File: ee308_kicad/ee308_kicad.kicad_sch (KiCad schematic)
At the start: 0 parts

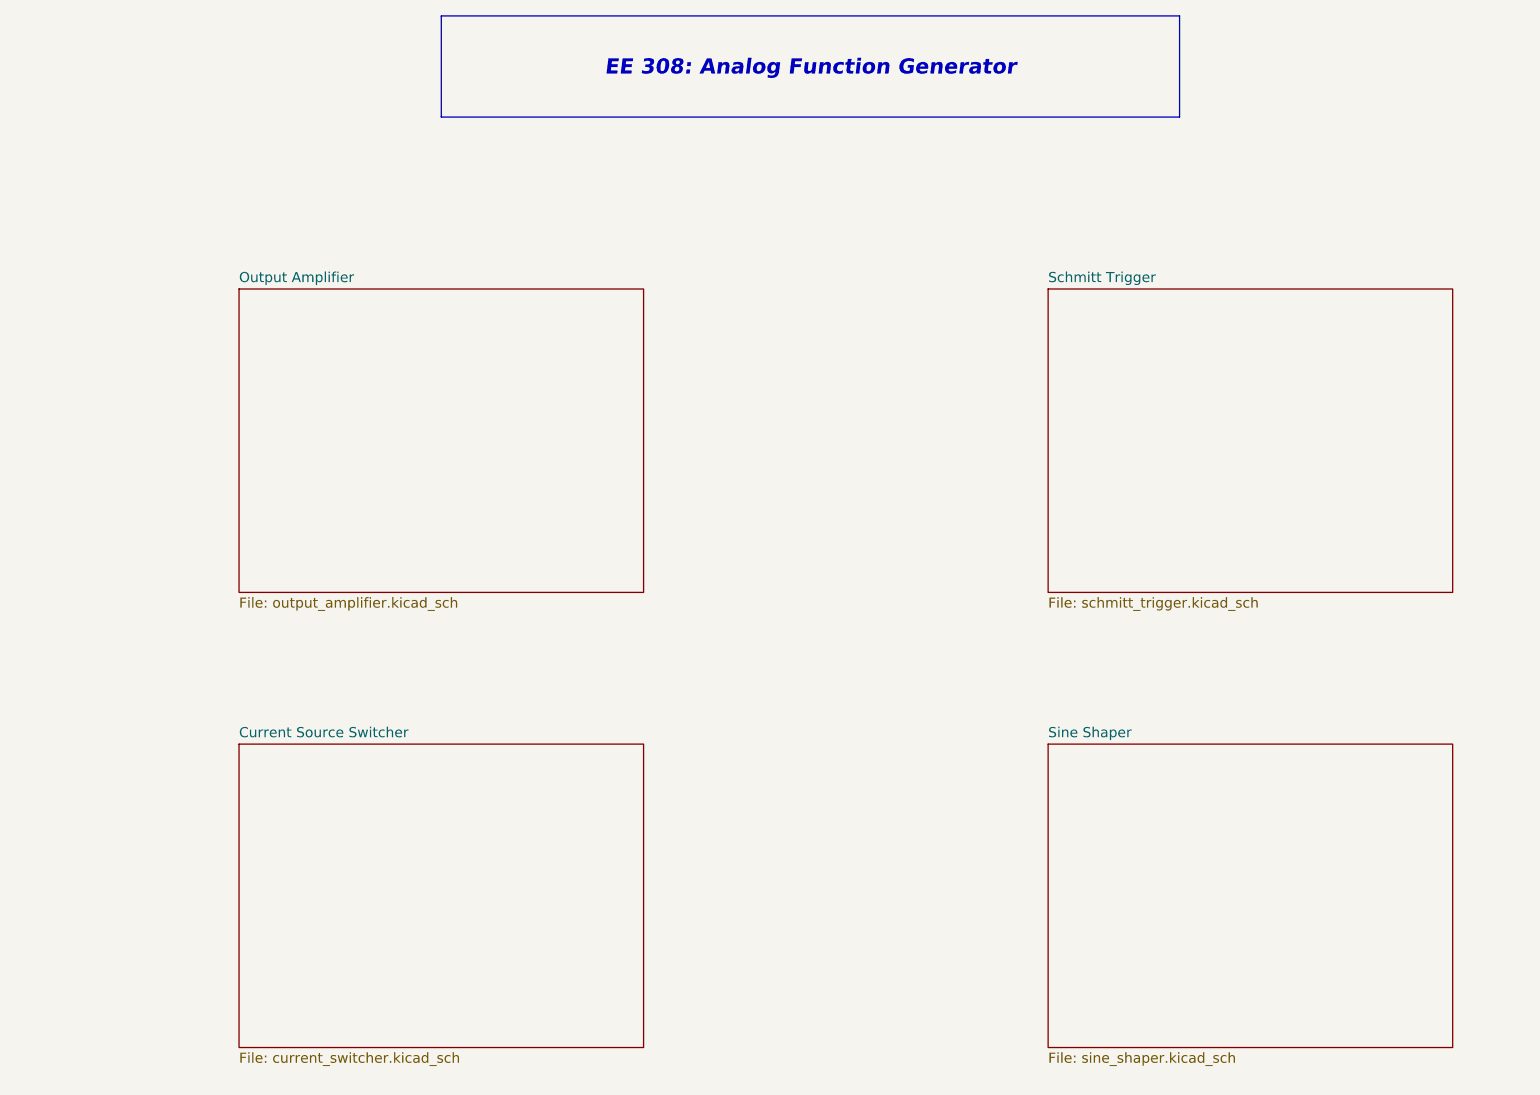
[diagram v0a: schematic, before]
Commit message: Update with current switch/integrator.
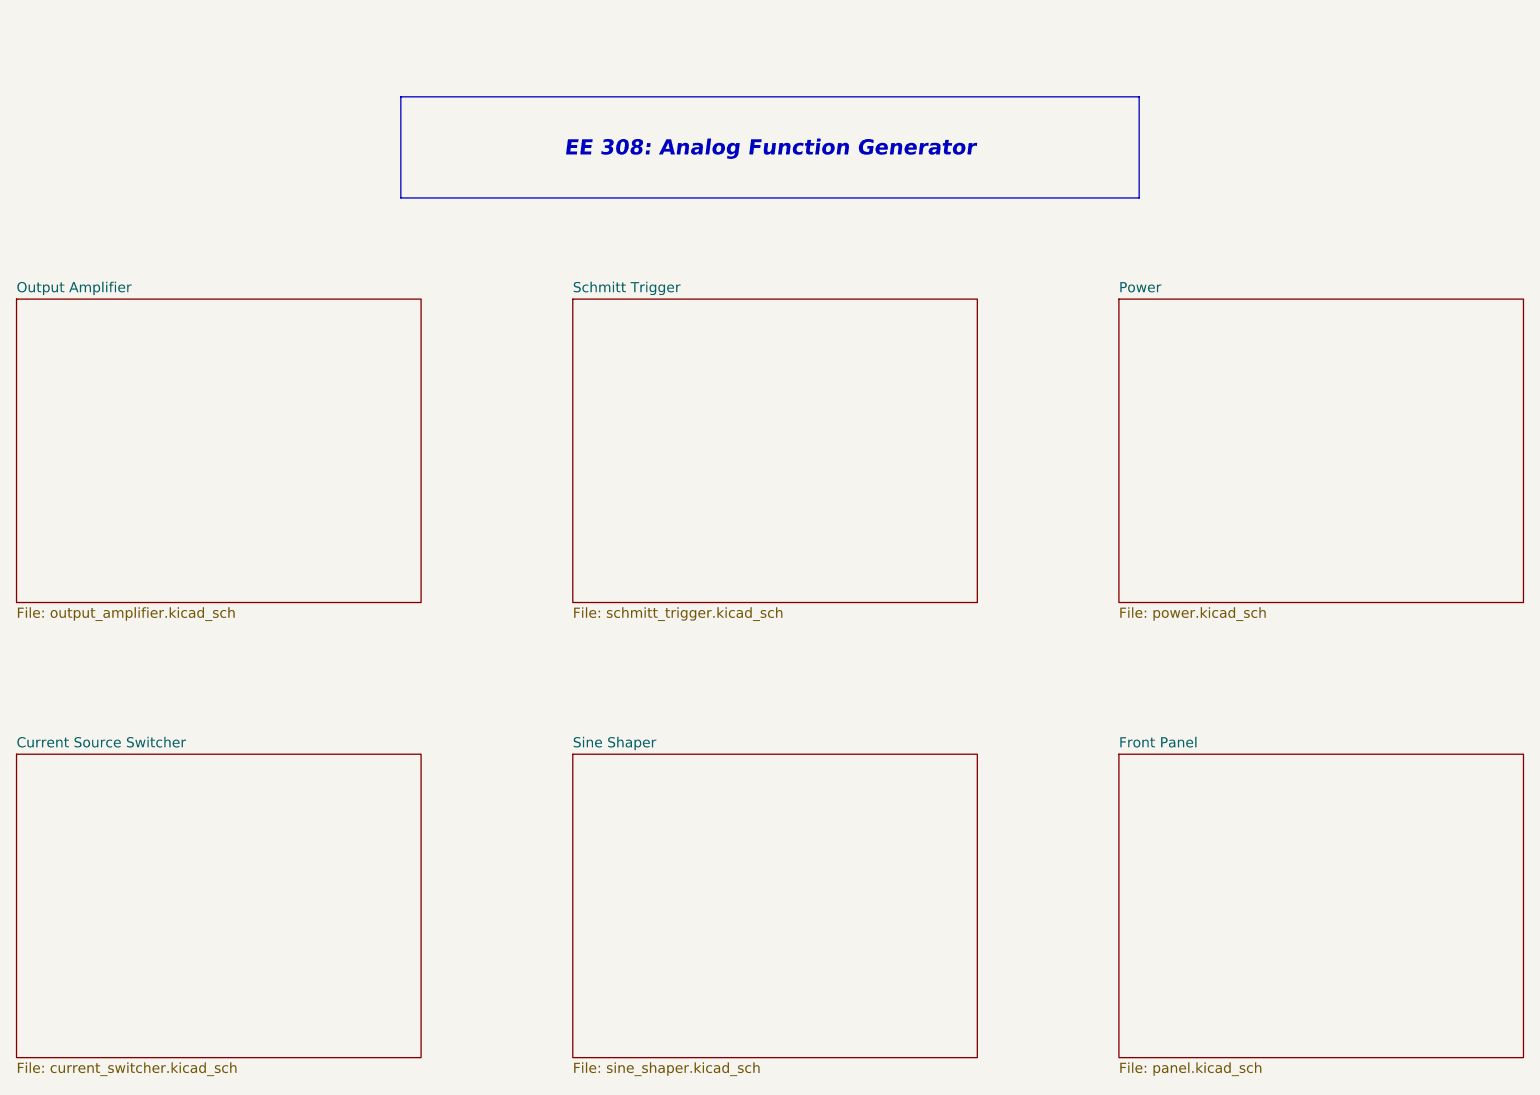
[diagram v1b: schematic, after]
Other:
- added sheet Front Panel (panel.kicad_sch)
- added sheet Power (power.kicad_sch)
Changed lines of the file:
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@@
 	(text_box "EE 308: Analog Function Generator"
 		(exclude_from_sim no)
-		(at 104.14 15.24 0)
+		(at 99.06 25.4 0)
 		(size 92.71 12.7)
 		(margins 0.9525 0.9525 0.9525 0.9525)
@@
 	)
 	(sheet
-		(at 180.34 106.68)
+		(at 120.65 107.95)
 		(size 50.8 38.1)
 		(exclude_from_sim no)
@@
 		)
 		(property "Sheetname" "Sine Shaper"
-			(at 180.34 105.9684 0)
+			(at 120.65 107.2384 0)
 			(effects
 				(font
@@
 		)
 		(property "Sheetfile" "sine_shaper.kicad_sch"
-			(at 180.34 145.3646 0)
+			(at 120.65 146.6346 0)
 			(effects
 				(font
@@
 		)
 		(property "Field2" ""
-			(at 180.34 106.68 0)
+			(at 120.65 107.95 0)
 			(effects
 				(font
@@
 	)
 	(sheet
-		(at 180.34 49.53)
+		(at 189.23 107.95)
+		(size 50.8 38.1)
+		(exclude_from_sim no)
+		(in_bom yes)
+		(on_board yes)
+		(dnp no)
+		(fields_autoplaced yes)
+		(stroke
+			(width 0.1524)
+			(type solid)
+		)
+		(fill
+			(color 0 0 0 0.0000)
+		)
+		(property "Sheetname" "Front Panel"
+			(at 189.23 107.2384 0)
+			(effects
+				(font
+					(size 1.27 1.27)
+				)
+				(justify left bottom)
+			)
+		)
+		(property "Sheetfile" "panel.kicad_sch"
+			(at 189.23 146.6346 0)
+			(effects
+				(font
+					(size 1.27 1.27)
+				)
+				(justify left top)
+			)
+		)
+		(instances
+			(project "ee308_kicad"
+				(path "/a3231158-6fd4-4190-9d01-56c0026ed088"
+					(page "7")
+				)
+			)
+		)
+	)
+	(sheet
+		(at 120.65 50.8)
 		(size 50.8 38.1)
 		(exclude_from_sim no)
@@
 		)
 		(property "Sheetname" "Schmitt Trigger"
-			(at 180.34 48.8184 0)
+			(at 120.65 50.0884 0)
 			(effects
 				(font
@@
 		)
 		(property "Sheetfile" "schmitt_trigger.kicad_sch"
-			(at 180.34 88.2146 0)
+			(at 120.65 89.4846 0)
 			(effects
 				(font
@@
 	)
 	(sheet
-		(at 78.74 49.53)
+		(at 50.8 50.8)
 		(size 50.8 38.1)
 		(exclude_from_sim no)
@@
 		)
 		(property "Sheetname" "Output Amplifier"
-			(at 78.74 48.8184 0)
+			(at 50.8 50.0884 0)
 			(show_name yes)
 			(effects
@@
 		)
 		(property "Sheetfile" "output_amplifier.kicad_sch"
-			(at 78.74 88.2146 0)
+			(at 50.8 89.4846 0)
 			(effects
 				(font
@@
 	)
 	(sheet
-		(at 78.74 106.68)
+		(at 50.8 107.95)
 		(size 50.8 38.1)
 		(exclude_from_sim no)
@@
 		)
 		(property "Sheetname" "Current Source Switcher"
-			(at 78.74 105.9684 0)
+			(at 50.8 107.2384 0)
 			(effects
 				(font
@@
 		)
 		(property "Sheetfile" "current_switcher.kicad_sch"
-			(at 78.74 145.3646 0)
+			(at 50.8 146.6346 0)
 			(effects
 				(font
@@
 				)
 			)
+		)
+	)
+	(sheet
+		(at 189.23 50.8)
+		(size 50.8 38.1)
+		(exclude_from_sim no)
+		(in_bom yes)
+		(on_board yes)
+		(dnp no)
+		(fields_autoplaced yes)
+		(stroke
+			(width 0.1524)
+			(type solid)
+		)
+		(fill
+			(color 0 0 0 0.0000)
+		)
+		(property "Sheetname" "Power"
+			(at 189.23 50.0884 0)
+			(effects
+				(font
+					(size 1.27 1.27)
+				)
+				(justify left bottom)
+			)
+		)
+		(property "Sheetfile" "power.kicad_sch"
+			(at 189.23 89.4846 0)
+			(effects
+				(font
+					(size 1.27 1.27)
+				)
+				(justify left top)
+			)
+		)
+		(instances
+			(project "ee308_kicad"
+				(path "/a3231158-6fd4-4190-9d01-56c0026ed088"
+					(page "6")
+				)
+			)
